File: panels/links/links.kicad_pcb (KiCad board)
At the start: 2 copper layers, 20 x 128.5 mm, 0 parts

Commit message: Links Panel Desgin
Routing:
- added copper zone on B.Cu, net (none)
- added copper zone on F.Cu, net (none)
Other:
- outline, holes or cut-outs redrawn
- board text added: "ADD"
- board text added: "IN"
- board text added: "Links"
- board text added: "MLT"
- board text added: "OUT"
- board text added: "SUM"
- board text added: "www.birchavenue.org"

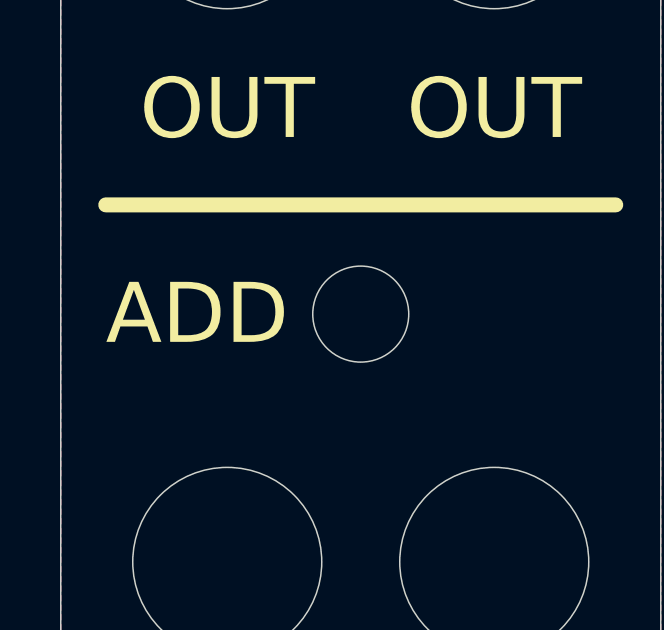
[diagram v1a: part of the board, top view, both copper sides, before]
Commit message: Relabel ADD as AVG
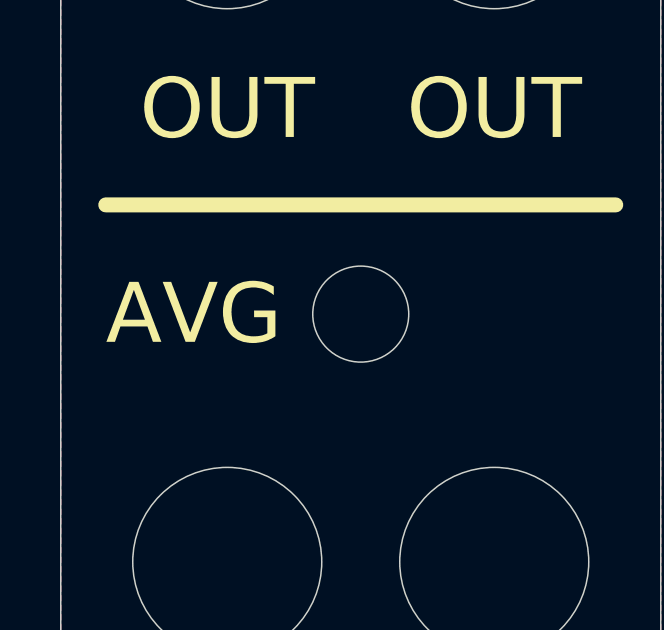
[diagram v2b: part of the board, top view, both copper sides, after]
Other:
- board text added: "AVG"
- board text removed: "ADD"
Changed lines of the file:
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@@
 		)
 	)
-	(gr_text "ADD"
+	(gr_text "AVG"
 		(at 81.5 141.64 0)
 		(layer "F.SilkS")
@@
 			(justify left)
 		)
-		(render_cache "ADD" 0
+		(render_cache "AVG" 0
 			(polygon
 				(pts
@@
 			(polygon
 				(pts
-					(xy 84.49777 140.425515) (xy 84.607665 140.445514) (xy 84.709308 140.478847) (xy 84.802697 140.525514)
-					(xy 84.887834 140.585513) (xy 84.964718 140.658845) (xy 84.993161 140.691912) (xy 85.057191 140.782124)
-					(xy 85.110369 140.882402) (xy 85.152694 140.992745) (xy 85.17874 141.088267) (xy 85.19784 141.190231)
-					(xy 85.209995 141.298637) (xy 85.215205 141.413484) (xy 85.215422 141.443203) (xy 85.211926 141.559577)
-					(xy 85.201439 141.669585) (xy 85.18396 141.773228) (xy 85.15949 141.870505) (xy 85.119071 141.983151)
-					(xy 85.067727 142.085849) (xy 85.00546 142.178602) (xy 84.991695 142.195959) (xy 84.917762 142.274906)
-					(xy 84.83579 142.340473) (xy 84.74578 142.392658) (xy 84.647733 142.431463) (xy 84.541647 142.456886)
-					(xy 84.427523 142.468929) (xy 84.379623 142.47) (xy 83.589253 142.47) (xy 83.589253 142.239434)
-					(xy 83.850593 142.239434) (xy 84.334682 142.239434) (xy 84.443469 142.232307) (xy 84.541953 142.210927)
-					(xy 84.643827 142.167967) (xy 84.731676 142.105606) (xy 84.795812 142.036713) (xy 84.849433 141.954166)
-					(xy 84.89196 141.858568) (xy 84.923393 141.749918) (xy 84.941113 141.649407) (xy 84.951128 141.539831)
-					(xy 84.953593 141.445645) (xy 84.949741 141.328115) (xy 84.938185 141.219768) (xy 84.918925 141.120604)
-					(xy 84.885643 141.013729) (xy 84.841267 140.920077) (xy 84.795812 140.852135) (xy 84.719985 140.773145)
-					(xy 84.630132 140.713556) (xy 84.526254 140.673368) (xy 84.426054 140.654363) (xy 84.334682 140.649413)
-					(xy 83.850593 140.649413) (xy 83.850593 142.239434) (xy 83.589253 142.239434) (xy 83.589253 140.418848)
-					(xy 84.379623 140.418848)
+					(xy 84.425052 142.47) (xy 84.143684 142.47) (xy 83.406071 140.418848) (xy 83.687438 140.418848)
+					(xy 84.289741 142.154926) (xy 84.858339 140.418848) (xy 85.136775 140.418848)
 				)
 			)
 			(polygon
 				(pts
-					(xy 86.451713 140.425515) (xy 86.561608 140.445514) (xy 86.66325 140.478847) (xy 86.75664 140.525514)
-					(xy 86.841777 140.585513) (xy 86.918661 140.658845) (xy 86.947103 140.691912) (xy 87.011134 140.782124)
-					(xy 87.064311 140.882402) (xy 87.106637 140.992745) (xy 87.132683 141.088267) (xy 87.151783 141.190231)
-					(xy 87.163938 141.298637) (xy 87.169147 141.413484) (xy 87.169364 141.443203) (xy 87.165869 141.559577)
-					(xy 87.155382 141.669585) (xy 87.137903 141.773228) (xy 87.113433 141.870505) (xy 87.073014 141.983151)
-					(xy 87.02167 142.085849) (xy 86.959402 142.178602) (xy 86.945638 142.195959) (xy 86.871704 142.274906)
-					(xy 86.789733 142.340473) (xy 86.699723 142.392658) (xy 86.601675 142.431463) (xy 86.49559 142.456886)
-					(xy 86.381466 142.468929) (xy 86.333565 142.47) (xy 85.543196 142.47) (xy 85.543196 142.239434)
-					(xy 85.804535 142.239434) (xy 86.288625 142.239434) (xy 86.397412 142.232307) (xy 86.495895 142.210927)
-					(xy 86.597769 142.167967) (xy 86.685619 142.105606) (xy 86.749755 142.036713) (xy 86.803376 141.954166)
-					(xy 86.845903 141.858568) (xy 86.877336 141.749918) (xy 86.895055 141.649407) (xy 86.905071 141.539831)
-					(xy 86.907536 141.445645) (xy 86.903684 141.328115) (xy 86.892128 141.219768) (xy 86.872867 141.120604)
-					(xy 86.839586 141.013729) (xy 86.79521 140.920077) (xy 86.749755 140.852135) (xy 86.673927 140.773145)
-					(xy 86.584075 140.713556) (xy 86.480197 140.673368) (xy 86.379996 140.654363) (xy 86.288625 140.649413)
-					(xy 85.804535 140.649413) (xy 85.804535 142.239434) (xy 85.543196 142.239434) (xy 85.543196 140.418848)
-					(xy 86.333565 140.418848)
+					(xy 85.543684 141.451507) (xy 85.547977 141.552121) (xy 85.560857 141.653379) (xy 85.563224 141.666929)
+					(xy 85.586545 141.763353) (xy 85.618582 141.856407) (xy 85.633565 141.893098) (xy 85.67968 141.984309)
+					(xy 85.735468 142.065846) (xy 85.76448 142.100216) (xy 85.838197 142.166975) (xy 85.921556 142.219582)
+					(xy 85.976971 142.246273) (xy 86.072253 142.27909) (xy 86.176078 142.298285) (xy 86.277878 142.303914)
+					(xy 86.37987 142.29768) (xy 86.489962 142.27465) (xy 86.590471 142.234649) (xy 86.681395 142.177678)
+					(xy 86.740474 142.126594) (xy 86.81128 142.044318) (xy 86.864694 141.952645) (xy 86.900718 141.851576)
+					(xy 86.919351 141.74111) (xy 86.922191 141.673768) (xy 86.922191 141.617592) (xy 86.297906 141.617592)
+					(xy 86.297906 141.386538) (xy 87.153244 141.386538) (xy 87.153244 142.481235) (xy 86.987159 142.481235)
+					(xy 86.922191 142.208171) (xy 86.847239 142.28465) (xy 86.768684 142.350931) (xy 86.686527 142.407015)
+					(xy 86.578764 142.462781) (xy 86.465373 142.502614) (xy 86.346352 142.526513) (xy 86.247082 142.534161)
+					(xy 86.221702 142.53448) (xy 86.120067 142.529824) (xy 86.023255 142.515856) (xy 85.909024 142.485302)
+					(xy 85.80233 142.440198) (xy 85.703173 142.380545) (xy 85.611553 142.306342) (xy 85.543684 142.236503)
+					(xy 85.482318 142.15917) (xy 85.429134 142.076402) (xy 85.384132 141.9882) (xy 85.347313 141.894563)
+					(xy 85.318675 141.795492) (xy 85.29822 141.690987) (xy 85.285947 141.581047) (xy 85.281856 141.465673)
+					(xy 85.285428 141.364053) (xy 85.296144 141.262158) (xy 85.307257 141.194075) (xy 85.330031 141.098598)
+					(xy 85.363425 141.000236) (xy 85.403 140.908311) (xy 85.450399 140.818771) (xy 85.504666 140.736387)
+					(xy 85.572295 140.654029) (xy 85.578855 140.646971) (xy 85.651956 140.580214) (xy 85.739368 140.520995)
+					(xy 85.830275 140.474142) (xy 85.863154 140.459881) (xy 85.955416 140.427183) (xy 86.053419 140.403827)
+					(xy 86.157161 140.389814) (xy 86.266643 140.385143) (xy 86.373499 140.38934) (xy 86.474249 140.401934)
+					(xy 86.58709 140.428129) (xy 86.691137 140.466414) (xy 86.786392 140.516789) (xy 86.84501 140.55709)
+					(xy 86.92391 140.626332) (xy 86.990617 140.705467) (xy 87.045131 140.794494) (xy 87.087452 140.893412)
+					(xy 87.117579 141.002222) (xy 87.124912 141.04069) (xy 86.857711 141.04069) (xy 86.824807 140.936526)
+					(xy 86.773355 140.845498) (xy 86.703357 140.767609) (xy 86.656454 140.730013) (xy 86.572404 140.680005)
+					(xy 86.479012 140.644284) (xy 86.376277 140.622852) (xy 86.278721 140.615819) (xy 86.2642 140.615708)
+					(xy 86.165249 140.621313) (xy 86.054881 140.642837) (xy 85.95365 140.680504) (xy 85.861556 140.734313)
+					(xy 85.778597 140.804266) (xy 85.740544 140.845296) (xy 85.673642 140.936412) (xy 85.620582 141.037935)
+					(xy 85.586939 141.130487) (xy 85.562909 141.230267) (xy 85.54849 141.337273)
 				)
 			)
